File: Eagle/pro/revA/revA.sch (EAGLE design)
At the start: 4 parts

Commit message: mcu part
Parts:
- added U$1: ATSAM4LSAA-AUR, atmel:ATSAM4LSAA-AUR
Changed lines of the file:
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@@
 <part name="H3" library="holes" deviceset="MOUNT-PAD-ROUND" device="3.0"/>
 <part name="H4" library="holes" deviceset="MOUNT-PAD-ROUND" device="3.0"/>
+<part name="U$1" library="atmel" deviceset="ATSAM4LSAA-AUR" device=""/>
 </parts>
 <sheets>
@@
 </plain>
 <instances>
+<instance part="U$1" gate="G$1" x="50.8" y="43.18"/>
 </instances>
 <busses>

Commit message: sort prog header
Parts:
- removed U$1: ATSAM4LSAA-AUR, atmel:ATSAM4LSAA-AUR
- added ATSAM4LS: ATSAM4LSAA-AUR, atmel:ATSAM4LSAA-AUR
- added C1: 100nF, SparkFun:CAP0805
- added C2, C3: 22pF, SparkFun:CAP0805
- added JTAG: (no value), con-lstb:MA05-2
- added Q1: 20MHz, SparkFun:CRYSTALHC49UV
- added R1, R2, R3: 100K, SparkFun:RESISTOR1206
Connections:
- new net 3.3V: C1.1, JTAG.1, R1.1, R2.1, R3.1
- new net GND: C1.2, C2.2, C3.2, JTAG.3, JTAG.5, JTAG.9
- new net N$1: ATSAM4LS.XOUT32, C3.1, Q1.2
- new net N$2: ATSAM4LS.XIN32, C2.1, Q1.1
- new net NRESET: ATSAM4LS.RESET_N, JTAG.10
- new net TCK: ATSAM4LS.TCK, JTAG.4, R2.2
- new net TDI: ATSAM4LS.PA24, JTAG.8, R3.2
- new net TDO: ATSAM4LS.PA23, JTAG.6
- new net TMS: ATSAM4LS.PA03, JTAG.2, R1.2

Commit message: op amps
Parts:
- added C4, C6: 22pF, SparkFun:CAP0805
- added R10, R4, R6, R7, R8, R9: 100K, SparkFun:RESISTOR1206
- added U$1, U$2: LM393, SparkFun:LM393
- added U$3: AUDIO-JACKPTH, SparkFun:AUDIO-JACKPTH
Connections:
- new net AUDIO_LEFT: ATSAM4LS.PA04, R4.2, U$1G1.OUT
- new net AUDIO_RIGHT: ATSAM4LS.PA05, R9.2, U$1G2.OUT
- new net N$10: U$1G1.V-, U$2G1.V-
- new net N$11: U$1G1.V+, U$2G1.V+
- new net N$12: U$2G1.+IN, U$3.2
- new net N$3: U$2G2.+IN, U$3.5
- new net N$4: R4.1, R6.2, U$1G1.-IN
- new net N$5: C6.1, R8.1, U$1G2.+IN
- new net N$6: C4.1, R7.1, U$1G1.+IN
- new net N$7: R8.2, U$2G2.-IN, U$2G2.OUT
- new net N$8: R7.2, U$2G1.-IN, U$2G1.OUT
- new net N$9: R10.2, R9.1, U$1G2.-IN
- net GND: now also C4.2, C6.2, R10.1, R6.1, U$3.1

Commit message: simplify
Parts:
- added C5, C7, C8, C9: (no value), SparkFun:CAP0805
- added R11, R12, R13: (no value), SparkFun:RESISTOR1206
- added R5: 100K, SparkFun:RESISTOR1206
- added U$4: LM393, SparkFun:LM393
- added U1: MCP42XXX, SparkFun:MCP42XXX
- added X1: USB-MB-H, SparkFun:USB-MB-H
- C4, C6: value 22pF -> (none)
- R10: value 100K -> (none)
- U$2: value LM393 -> AUDIO-JACKPTH; device SparkFun:LM393 -> SparkFun:AUDIO-JACKPTH
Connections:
- new net DIGI_POT_RST: U1.RST
- new net DIGI_POT_SHDW: U1.SHTDWN
- new net DIGI_RES_LEFT: R4.1, U$1G1.-IN, U1.A1
- new net DIGI_RES_RIGHT: R9.1, U$1G2.-IN, U1.A0
- new net DIG_POT_CS: U1.CS
- new net MISO: ATSAM4LS.PA27, U1.DO
- new net MOSI: ATSAM4LS.PA28, U1.DI
- new net N$13: R13.1
- new net N$14: R12.1
- new net RAW_LEFT: C4.1, U$3.5
- new net RAW_RIGHT: C5.1, U$3.2
- new net SCLK: ATSAM4LS.PA29, U1.SCK
- new net USB_D+: ATSAM4LS.PS26, R10.1
- new net USB_D-: ATSAM4LS.PA25, R11.1
- new net VCC: R5.2, R8.2, U$1G1.V+, U1.VCC, X1.VBUS
- net GND: now also C7.2, R7.1, U$1G1.V-, U$2.1, U1.B0, U1.B1, U1.GND, U1.W0, U1.W1, X1.GND; no longer C4.2, R10.1
- net N$10: now also C6.1, R13.2, U$4G1.+IN; no longer U$1G1.V-, U$2G1.V-
- net N$11: now also C7.1, R12.2, U$4G2.+IN; no longer U$1G1.V+, U$2G1.V+
- net N$12: now also C8.2, U$2.5; no longer U$2G1.+IN, U$3.2
- net N$3: now also R11.2, X1.D-; no longer U$2G2.+IN, U$3.5
- net N$4: now also R10.2, X1.D+; no longer R4.1, R6.2, U$1G1.-IN
- net N$5: now also C5.2, R7.2; no longer C6.1
- net N$6: now also C4.2, R5.1, R6.2; no longer C4.1, R7.1
- net N$7: now also C9.1, U$4G2.-IN, U$4G2.OUT; no longer R8.2, U$2G2.-IN, U$2G2.OUT
- net N$8: now also C9.2, U$2.2; no longer R7.2, U$2G1.-IN, U$2G1.OUT
- net N$9: now also C8.1, U$4G1.-IN, U$4G1.OUT; no longer R10.2, R9.1, U$1G2.-IN

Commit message: sch done now routing
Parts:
- removed X1: USB-MB-H, SparkFun:USB-MB-H
- added C10, C11, C12, C13, C14, C15, C16, C17: 100nF, SparkFun:CAP0805
- added JP1: USB-MICROB, SparkFun-Connectors:USB-MICROB
- added JP2: JUMPER-3PTH, SparkFun:JUMPER-3PTH
- added R14, R15, R16: 100K, SparkFun:RESISTOR1206
- added S1, S2, S3: SWITCH-MOMENTARY-2PTH, SparkFun:SWITCH-MOMENTARY-2PTH
- added SV1, SV2, SV3, SV4: (no value), con-lstb:MA05-2
- added U$5: NHD_128X32, newhaven:NHD_128X32
- added U$6: POTTRIM, SparkFun:POTTRIM
- added U$7: V_REG_317SMD, SparkFun:V_REG_317SMD
- C4, C5, C8, C9: value (none) -> 100nF
- C6, C7: value (none) -> 22pF
- R10, R11: value (none) -> 68R
- R12, R13: value (none) -> 330K
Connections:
- removed net 3.3V: C1.1, JTAG.1, R1.1, R2.1, R3.1
- removed net DIGI_POT_RST: U1.RST
- removed net DIGI_POT_SHDW: U1.SHTDWN
- new net DAC_LEFT: ATSAM4LS.PA17, R13.1
- new net DAC_RIGHT: ATSAM4LS.PA19, R12.1
- new net DIG_POT_RST: ATSAM4LS.PA22, U1.RST
- new net DIG_POT_SHDW: ATSAM4LS.PA21, U1.SHTDWN
- new net LCD_AD: ATSAM4LS.PA00, SV3.5, SV4.6
- new net LCD_CS: ATSAM4LS.PA01, SV3.1, SV4.10
- new net LCD_RST: ATSAM4LS.PA02, SV3.3, SV4.8
- new net MCU_IN: ATSAM4LS.PA11, JP2.2
- new net MCU_OUT: ATSAM4LS.PA12, JP2.1
- new net N$15: C10.1, U$5.V0
- new net N$16: C11.1, U$5.V1
- new net N$17: C12.1, U$5.V2
- new net N$18: C13.1, U$5.V3
- new net N$19: C14.1, U$5.V4
- new net N$20: ATSAM4LS.PA08, R16.2, S3.2
- new net N$21: SV1.10, SV1.8, SV2.1, SV2.3, U$5.VDD
- new net N$22: C10.2, C11.2, C12.2, C13.2, C14.2, C17.2, SV1.2, SV1.4, SV1.6, SV2.5, SV2.7, SV2.9, U$5.VSS
- new net N$23: C15.2, U$5.C2-
- new net N$24: C15.1, U$5.C2+
- new net N$25: C16.2, U$5.C1+
- new net N$26: C16.1, U$5.C1-
- new net N$27: C17.1, U$5.VOUT
- new net N$28: SV1.1, SV2.10, U$5./CS1
- new net N$29: SV1.3, SV2.8, U$5./RST
- new net N$30: SV1.5, SV2.6, U$5.A0
- new net N$31: SV1.7, SV2.4, U$5.SCL
- new net N$32: SV1.9, SV2.2, U$5.SI
- new net N$33: JP1.VBUS, U$7.IN
- net DIG_POT_CS: now also ATSAM4LS.PA20
- net GND: now also ATSAM4LS.GND1, ATSAM4LS.GND2, ATSAM4LS.GND3, ATSAM4LS.GNDANA, JP1.GND, JP2.3, S1.1, S2.1, S3.1, SV3.2, SV3.4, SV3.6, SV4.5, SV4.7, SV4.9, U$4G1.V-, U$6.E, U$7.ADJ; no longer X1.GND
- net MOSI: now also SV3.9, SV4.2
- net N$13: now also ATSAM4LS.PA06, U$6.S; no longer R13.1
- net N$14: now also ATSAM4LS.PA09, R15.2, S2.2; no longer R12.1
- net N$3: now also JP1.D-; no longer X1.D-
- net N$4: now also JP1.D+; no longer X1.D+
- net NRESET: now also R14.2, S1.2
- net SCLK: now also SV3.7, SV4.4
- net VCC: now also ATSAM4LS.ADVREFP, ATSAM4LS.VDDANA, ATSAM4LS.VDDCORE, ATSAM4LS.VDDIN, ATSAM4LS.VDDIO1, ATSAM4LS.VDDIO2, ATSAM4LS.VDDIO3, ATSAM4LS.VDDOUT, C1.1, JTAG.1, R1.1, R14.1, R15.1, R16.1, R2.1, R3.1, SV3.10, SV3.8, SV4.1, SV4.3, U$4G1.V+, U$6.A, U$7.OUT; no longer X1.VBUS

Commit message: silkscreen
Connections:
- net N$22 renamed LCD_GND
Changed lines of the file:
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@@
 </segment>
 </net>
-<net name="N$22" class="0">
+<net name="LCD_GND" class="0">
 <segment>
 <pinref part="SV1" gate="G$1" pin="6"/>
@@
 <wire x1="76.2" y1="104.14" x2="76.2" y2="76.2" width="0.1524" layer="91"/>
 <junction x="76.2" y="76.2"/>
+<label x="93.98" y="58.42" size="1.778" layer="95"/>
 </segment>
 </net>

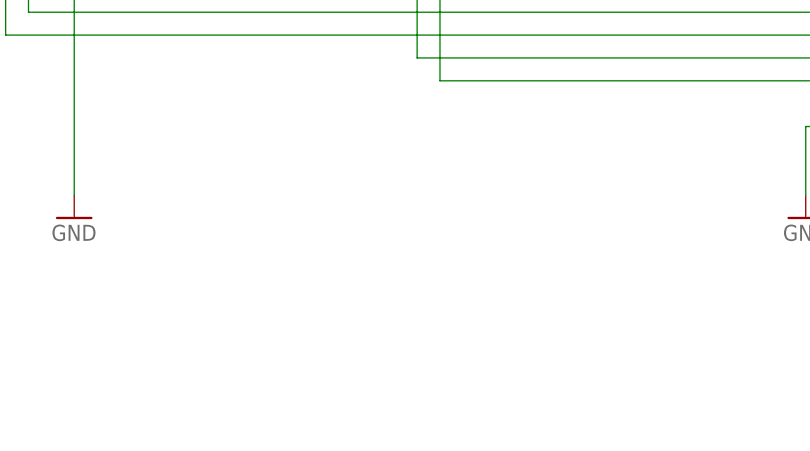
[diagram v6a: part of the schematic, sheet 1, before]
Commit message: tracking thickening and silkscreen tidy
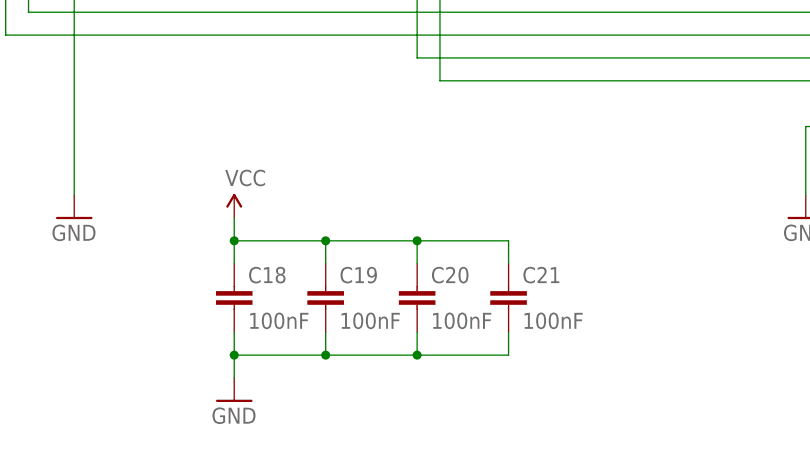
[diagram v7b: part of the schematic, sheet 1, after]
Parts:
- added C18, C19, C20, C21: 100nF, SparkFun:CAP0805
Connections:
- net GND: now also C18.2, C19.2, C20.2, C21.2
- net VCC: now also C18.1, C19.1, C20.1, C21.1
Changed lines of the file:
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@@
 <part name="P+9" library="SparkFun" deviceset="VCC" device=""/>
 <part name="GND15" library="SparkFun" deviceset="GND" device=""/>
+<part name="C18" library="SparkFun" deviceset="CAP" device="0805" value="100nF"/>
+<part name="C19" library="SparkFun" deviceset="CAP" device="0805" value="100nF"/>
+<part name="C20" library="SparkFun" deviceset="CAP" device="0805" value="100nF"/>
+<part name="C21" library="SparkFun" deviceset="CAP" device="0805" value="100nF"/>
+<part name="GND16" library="SparkFun" deviceset="GND" device=""/>
+<part name="P+10" library="SparkFun" deviceset="VCC" device=""/>
 </parts>
 <sheets>
@@
 <instance part="GND13" gate="1" x="180.34" y="129.54"/>
 <instance part="U$6" gate="G$1" x="241.3" y="109.22" rot="R180"/>
+<instance part="C18" gate="G$1" x="99.06" y="20.32"/>
+<instance part="C19" gate="G$1" x="109.22" y="20.32"/>
+<instance part="C20" gate="G$1" x="119.38" y="20.32"/>
+<instance part="C21" gate="G$1" x="129.54" y="20.32"/>
+<instance part="GND16" gate="1" x="99.06" y="10.16"/>
+<instance part="P+10" gate="1" x="99.06" y="30.48"/>
 </instances>
 <busses>
@@
 <pinref part="JP2" gate="G$1" pin="3"/>
 <wire x1="180.34" y1="132.08" x2="180.34" y2="134.62" width="0.1524" layer="91"/>
+</segment>
+<segment>
+<pinref part="GND16" gate="1" pin="GND"/>
+<pinref part="C18" gate="G$1" pin="2"/>
+<wire x1="99.06" y1="12.7" x2="99.06" y2="15.24" width="0.1524" layer="91"/>
+<pinref part="C21" gate="G$1" pin="2"/>
+<wire x1="99.06" y1="15.24" x2="99.06" y2="17.78" width="0.1524" layer="91"/>
+<wire x1="129.54" y1="17.78" x2="129.54" y2="15.24" width="0.1524" layer="91"/>
+<wire x1="129.54" y1="15.24" x2="119.38" y2="15.24" width="0.1524" layer="91"/>
+<junction x="99.06" y="15.24"/>
+<pinref part="C19" gate="G$1" pin="2"/>
+<wire x1="119.38" y1="15.24" x2="109.22" y2="15.24" width="0.1524" layer="91"/>
+<wire x1="109.22" y1="15.24" x2="99.06" y2="15.24" width="0.1524" layer="91"/>
+<wire x1="109.22" y1="17.78" x2="109.22" y2="15.24" width="0.1524" layer="91"/>
+<junction x="109.22" y="15.24"/>
+<pinref part="C20" gate="G$1" pin="2"/>
+<wire x1="119.38" y1="17.78" x2="119.38" y2="15.24" width="0.1524" layer="91"/>
+<junction x="119.38" y="15.24"/>
 </segment>
 </net>
@@
 <junction x="231.14" y="142.24"/>
 </segment>
-</net>
+<segment>
+<pinref part="C18" gate="G$1" pin="1"/>
+<pinref part="P+10" gate="1" pin="VCC"/>
+<wire x1="99.06" y1="25.4" x2="99.06" y2="27.94" width="0.1524" layer="91"/>
+<pinref part="C21" gate="G$1" pin="1"/>
+<wire x1="99.06" y1="27.94" x2="99.06" y2="30.48" width="0.1524" layer="91"/>
+<wire x1="129.54" y1="25.4" x2="129.54" y2="27.94" width="0.1524" layer="91"/>
+<wire x1="129.54" y1="27.94" x2="119.38" y2="27.94" width="0.1524" layer="91"/>
+<junction x="99.06" y="27.94"/>
+<pinref part="C19" gate="G$1" pin="1"/>
+<wire x1="119.38" y1="27.94" x2="109.22" y2="27.94" width="0.1524" layer="91"/>
+<wire x1="109.22" y1="27.94" x2="99.06" y2="27.94" width="0.1524" layer="91"/>
+<wire x1="109.22" y1="25.4" x2="109.22" y2="27.94" width="0.1524" layer="91"/>
+<junction x="109.22" y="27.94"/>
+<pinref part="C20" gate="G$1" pin="1"/>
+<wire x1="119.38" y1="25.4" x2="119.38" y2="27.94" width="0.1524" layer="91"/>
+<junction x="119.38" y="27.94"/>
+</segment>
+</net>
